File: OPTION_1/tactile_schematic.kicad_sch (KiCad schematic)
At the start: 58 parts, among them IC1 CY8C4145PVI-PS431, J1 Conn_01x02, J2 Conn_01x04, J3 Conn_01x04, J4 Conn_01x02, J5 Conn_ARM_SWD_TagConnect_TC203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

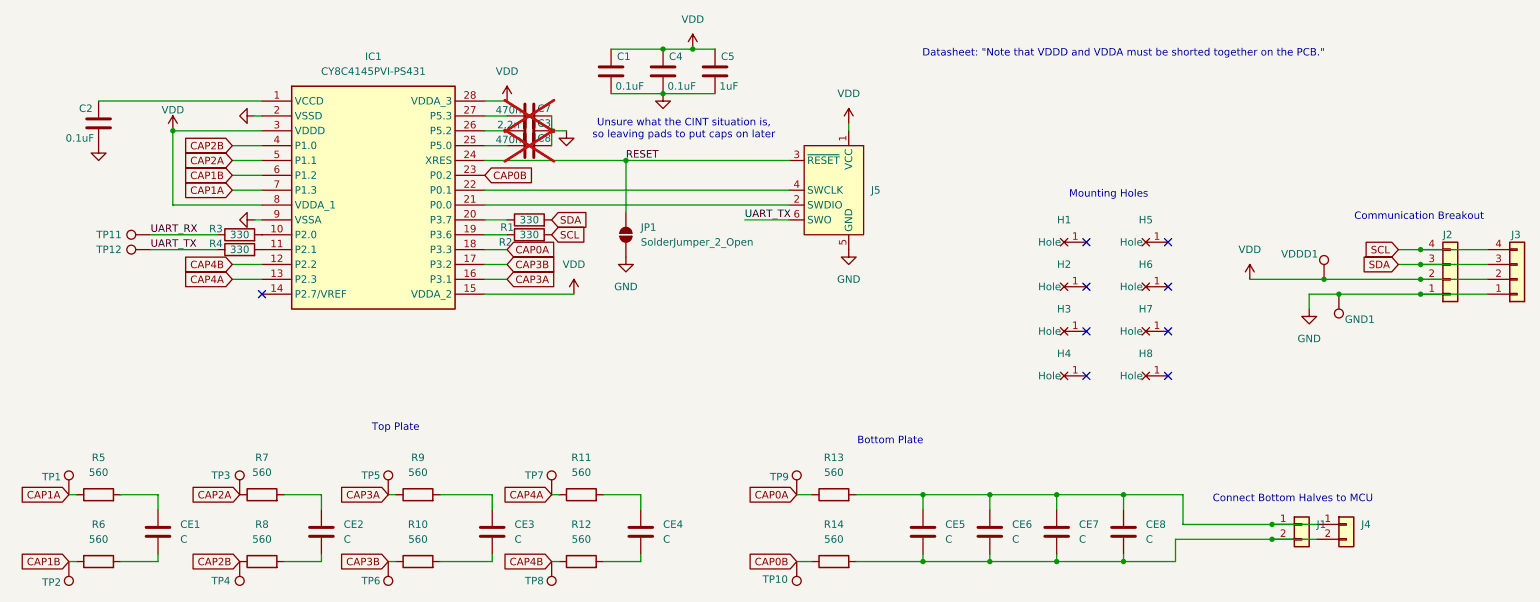
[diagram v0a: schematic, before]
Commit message: - remove RST pad - change all resistors to 560ohm - remove UART test points - relayout with cleaning - conosolidate down to 3 capacitor values (replace 1uf w/ paralel 2 470ufs) - add power LED - move b2b connector to be more convinient to solder wire to - make shield driven from pin - add SHIELD to b2b connector
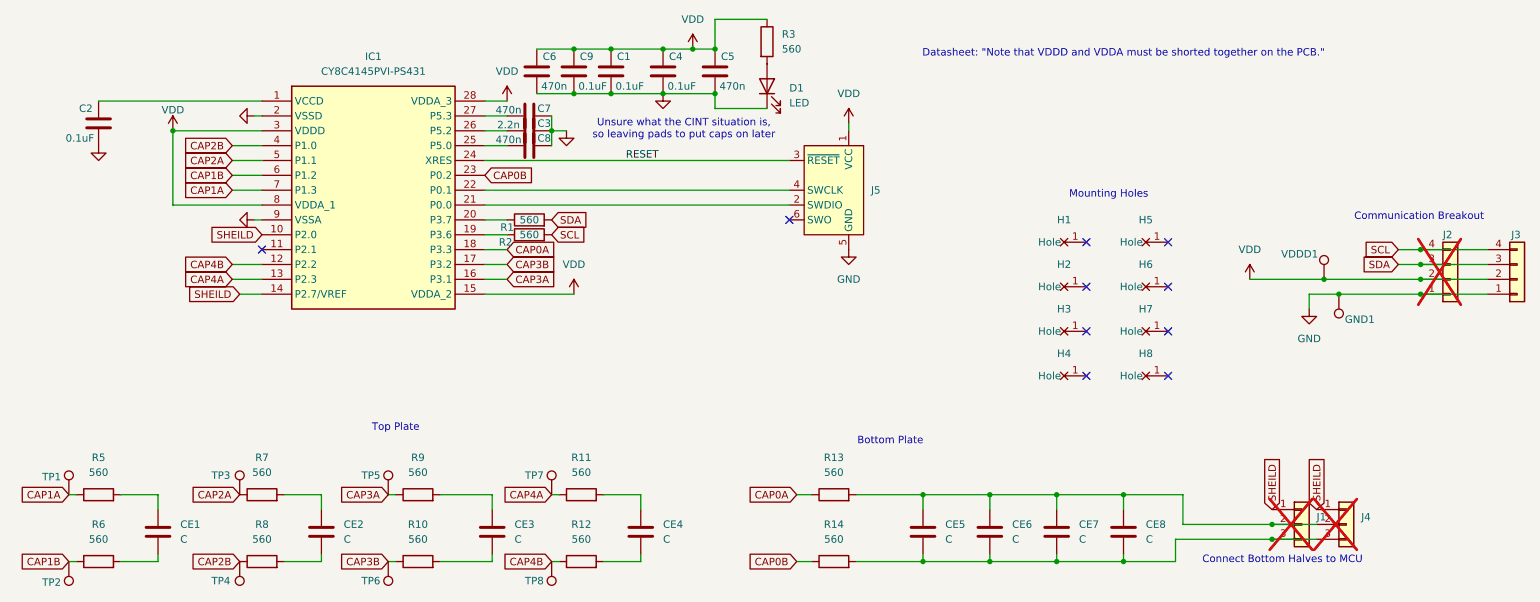
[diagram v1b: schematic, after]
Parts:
- removed JP1: SolderJumper_2_Open, Jumper:SolderJumper-2_P1.3mm_Open_Pad1.0x1.5mm, symbol Jumper:SolderJumper_2_Open
- removed R4: 330, Resistor_SMD:R_0603_1608Metric_Pad0.98x0.95mm_HandSolder, symbol Device:R
- removed TP10, TP11, TP12, TP9: TestPoint, TestPoint:TestPoint_THTPad_D1.0mm_Drill0.5mm, symbol Connector:TestPoint
- added C6: 470n, Capacitor_SMD:C_0603_1608Metric_Pad1.08x0.95mm_HandSolder, symbol ECE445L:C
- added C9: 0.1uF, Capacitor_SMD:C_0603_1608Metric_Pad1.08x0.95mm_HandSolder, symbol ECE445L:C
- added D1: LED, LED_SMD:LED_0603_1608Metric, symbol Device:LED
- C5: value 1uF -> 470n
- C7, C8: now fitted
- J1, J4: value Conn_01x02 -> Conn_01x03; footprint Connector_PinHeader_2.00mm:PinHeader_1x02_P2.00mm_Vertical -> Connector_PinHeader_2.00mm:PinHeader_1x03_P2.00mm_Vertical; symbol Connector_Generic:Conn_01x02 -> Connector_Generic:Conn_01x03; now not fitted
- J2: now not fitted
- R1, R2, R3: value 330 -> 560
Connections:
- net UART_RX is gone; now on net VDD: R3.1
- net GND: now also C6.2, C9.2, D1.1 (K)
- net VDD: now also C6.1, C9.1
- net at CE5.1, CE6.1, CE7.1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: now also J1.2 (Pin_2), J4.2 (Pin_2); no longer J1.1 (Pin_1), J4.1 (Pin_1)
- net at CE5.2, CE6.2, CE7.2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: now also J1.3 (Pin_3), J4.3 (Pin_3); no longer J1.2 (Pin_2), J4.2 (Pin_2)
- net at R3.2: now also D1.2 (A); no longer IC1.10 (P2.0)
- net SHEILD: now reaches IC1.14 (P2.7/VREF)
- net SHEILD: now also IC1.10 (P2.0), J1.1 (Pin_1), J4.1 (Pin_1)
- net UART_TX: no longer names the net of J5.6 (SWO)
- no-connect marks 9 -> 10
